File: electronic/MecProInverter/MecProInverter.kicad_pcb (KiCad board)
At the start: 4 copper layers, 104 x 175 mm, 167 parts, among them J10 Net, J3 ISO_Data, J4 Motor, J5 Display, J6 MAX312820, J7 Test, J8 U_ZK, J9 U_VS, K2 RT314A12, Q1 DMN3404L, Q2 DMN3404L, SW1 PTS645SM95SMTR92LFS, SW2 PTS645SM95SMTR92LFS, SW3 PTS645SM95SMTR92LFS, U1 ESP32-S3-MINI-1-N8, U10 CC6904SO-30A, U11 CC6904SO-30A, U12 TEA1-0505HI, U13 IKCM20L60GA, U14 PSRV05-4MR6T1G, U15 ADUM1201ARZ-RL7, U16 ADUM1201ARZ-RL7, U17 PSRV05-4MR6T1G, U18 PMV100EPAR, U19 PSRV05-4MR6T1G, U2 ADUM3160, U20 PSRV05-4MR6T1G, U3 TYPE-C_16PIN_2MD(073), U4 LVE2560E, U5 TPS563201DDCR, U6 SKRKAEE020, U7 SKRKAEE020, U8 TLA2528IRTER, U9 CC6904SO-30A

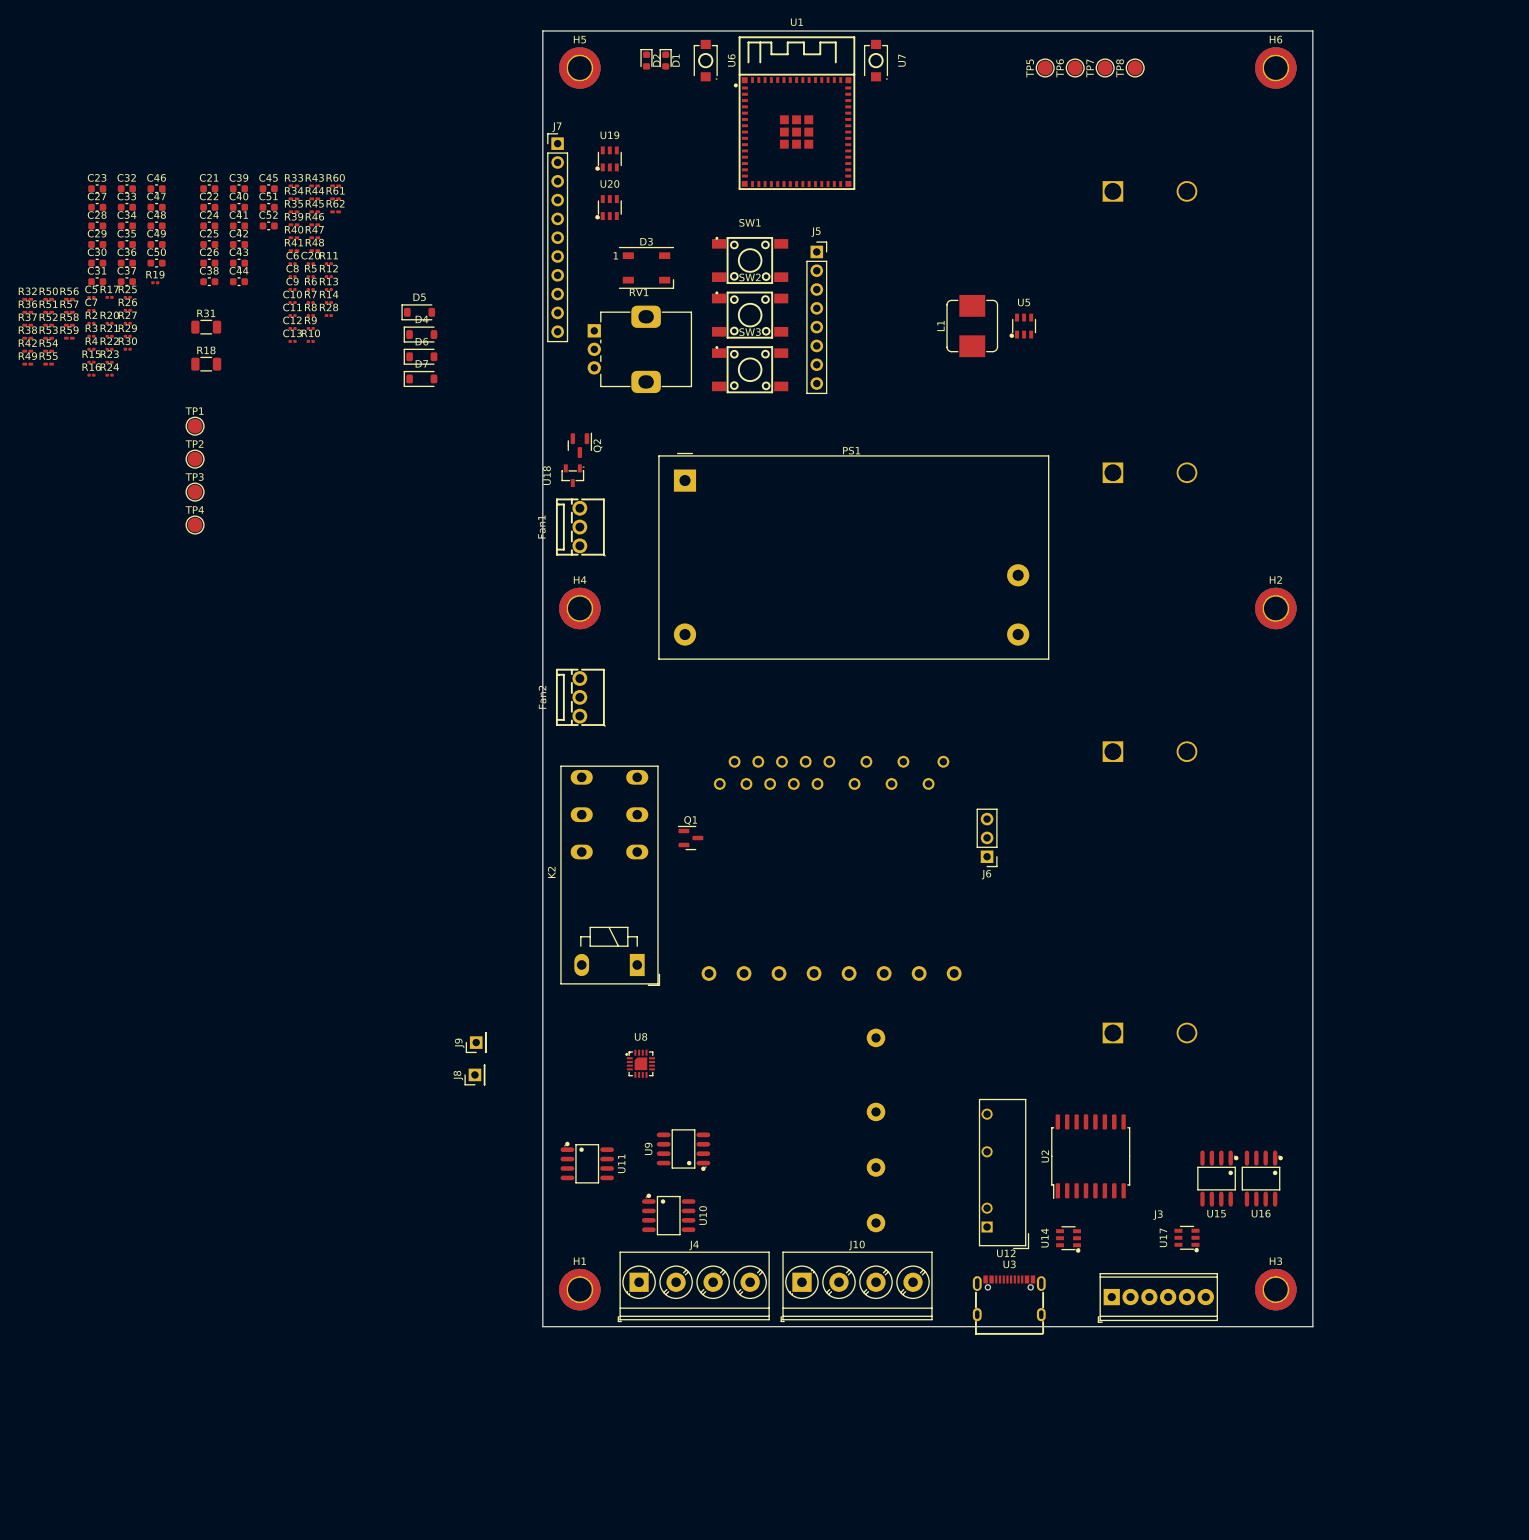
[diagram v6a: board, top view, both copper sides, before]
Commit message: Electronic
Voltage messurment updated
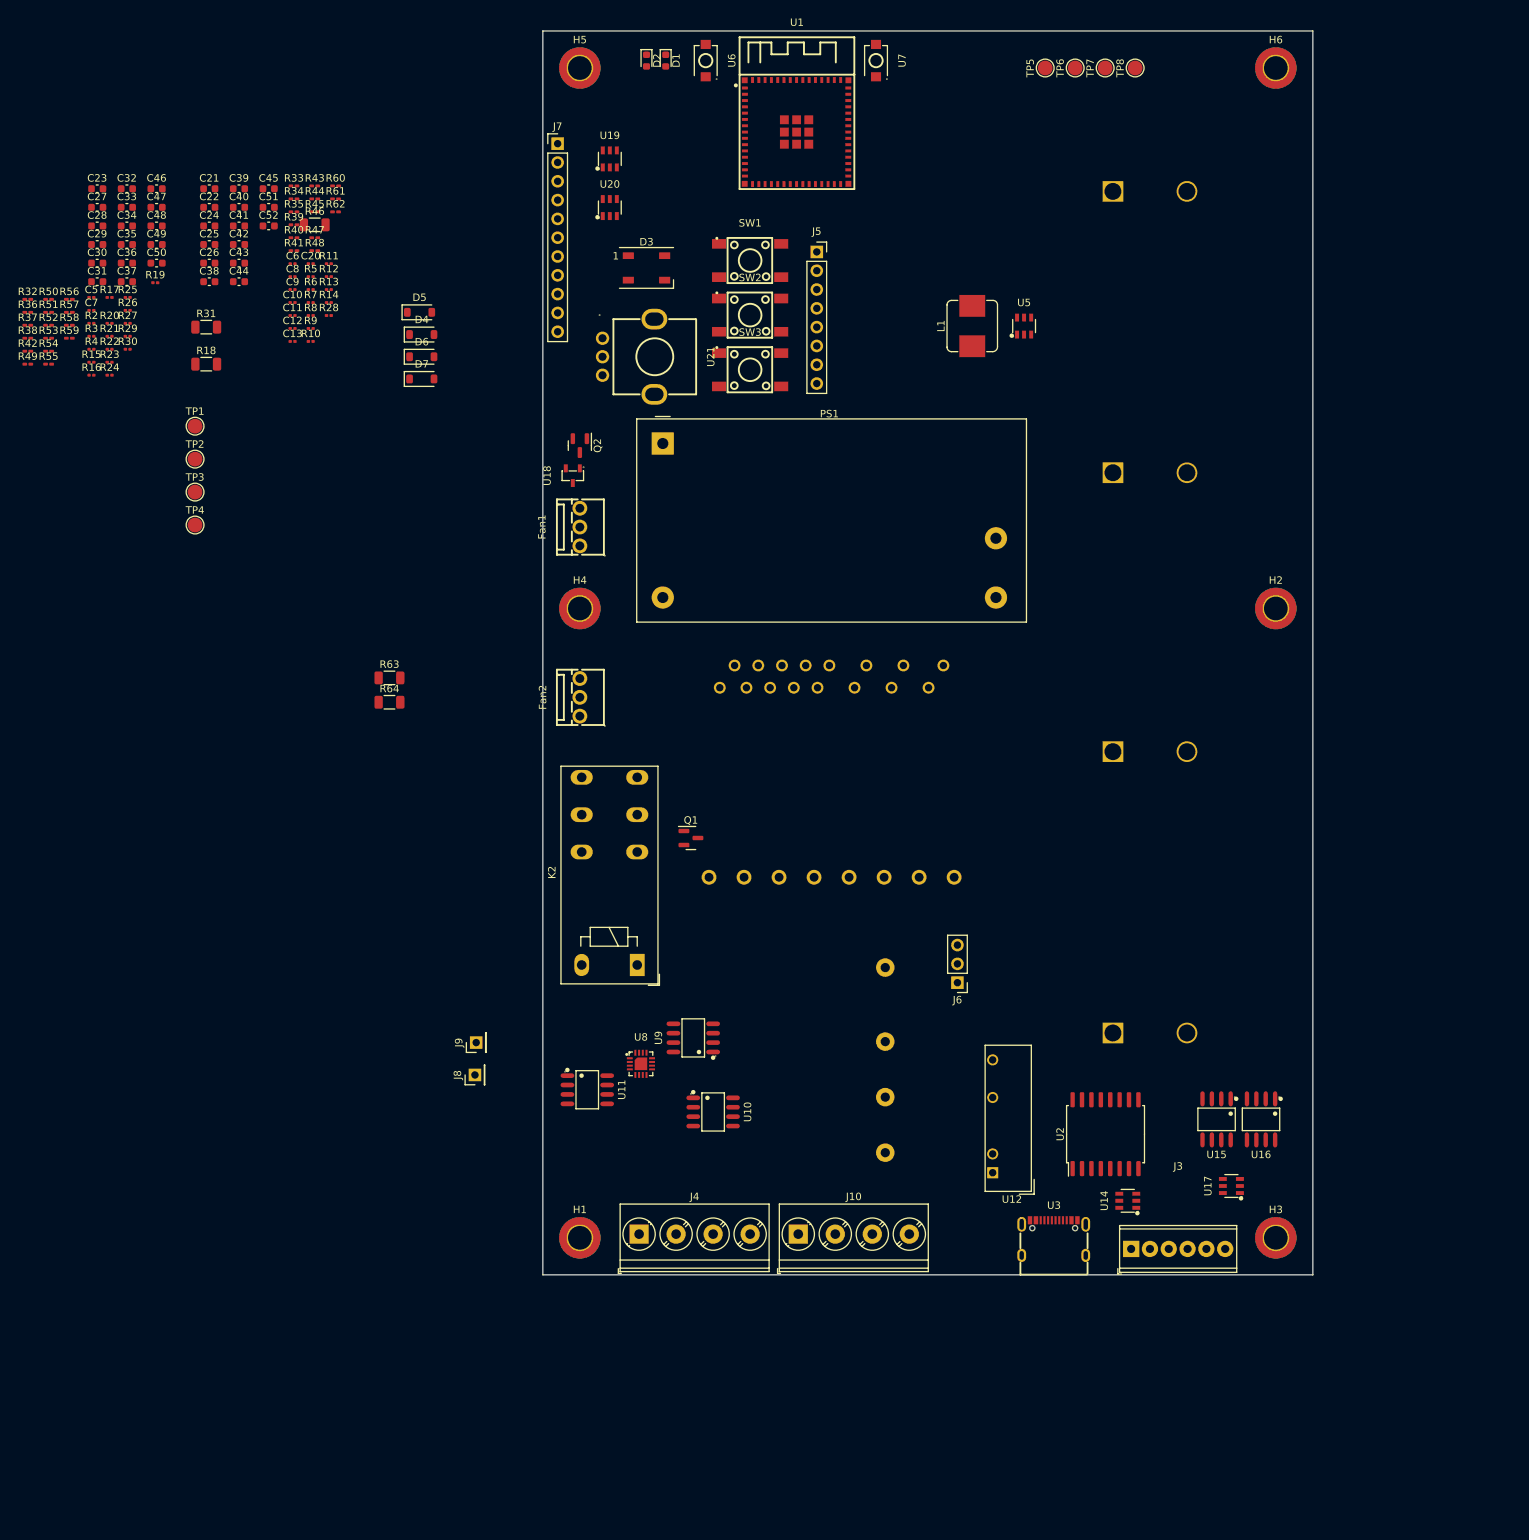
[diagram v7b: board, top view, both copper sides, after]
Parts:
- removed RV1: 10K, Potentiometer_THT:Potentiometer_Alps_RK09K_Single_Vertical
- added R63: 33k, Resistor_SMD:R_1206_3216Metric, F.Cu at (73.3, 140.4)
- added R64: 33k, Resistor_SMD:R_1206_3216Metric, F.Cu at (73.3, 143.7)
- added U21: RK09D113000F_10k, footprint:RES-ADJ-TH_RK09D1130C4G, F.Cu at (105.6, 97.0)
- R41: value 10k -> 4,7k
- R46: value 100k -> 33k; footprint Resistor_SMD:R_0201_0603Metric_Pad0.64x0.40mm_HandSolder -> Resistor_SMD:R_1206_3216Metric
- moved J6 17.5 mm to (150.0, 181.5)
- moved U10 15.2 mm to (117.0, 199.0)
- moved U9 15.1 mm to (114.3, 189.0)
- moved U13 13.0 mm to (133.0, 153.0)
- moved U11 10.0 mm to (100.0, 196.0)
- moved U3 10.0 mm to (163.0, 216.0)
- moved U4 9.58 mm to (140.2, 179.5)
- moved U14 9.46 mm to (173.0, 211.0)
- moved U17 9.22 mm to (187.0, 209.0)
- moved U15 8.00 mm to (185.0, 200.0)
- moved U16 8.00 mm to (191.0, 200.0)
- moved U12 7.37 mm to (154.8, 207.2)
- moved J3 7.01 mm to (173.5, 217.5)
- moved H1 7.00 mm to (99.0, 216.0)
- moved H3 7.00 mm to (193.0, 216.0)
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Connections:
- C51 pad 1: ITRIP -> Net-(U13-ITRIP)
- K2 pad 14: Net-(K2-Pad14) -> Net-(U4-~Phase)
- R41 pad 2: ITRIP -> Net-(U13-ITRIP)
- R46 pad 1: Net-(J8-Pin_1) -> Net-(R46-Pad1)
- R46 pad 2: Net-(U8-AIN2/GPIO2) -> Net-(R46-Pad2)
- U1 pad 27: VFO -> /Control/FAN2_PWM_FB
- U1 pad 30: unconnected-(U1-IO48-Pad30) -> /Control/FAN1_PWM_FB
- U1 pad 6: /Control/FAN1_PWM_FB -> VFO
- U1 pad 7: /Control/FAN2_PWM_FB -> unconnected-(U1-IO3-Pad7)
- U13 pad 15: ITRIP -> Net-(U13-ITRIP)
- U4 pad 1: Net-(J8-Pin_1) -> Net-(U4-VDD)
- U9 pad 1: Net-(K2-Pad14) -> Net-(U4-VDD)
- U9 pad 2: Net-(K2-Pad14) -> Net-(U4-VDD)
- U9 pad 3: Net-(U4-~Phase) -> Net-(J8-Pin_1)
- U9 pad 4: Net-(U4-~Phase) -> Net-(J8-Pin_1)
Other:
- board size 104 x 175 mm -> 104 x 168 mm

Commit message: Electronic
docu
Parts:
- C1, C2, C3, C4: footprint footprints:ESMQ351VSN102MA50S -> Own_Footprint:ESMQ351VSN102MA50S
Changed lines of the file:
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@@
     )
   )
-  (footprint "footprints:ESMQ351VSN102MA50S" locked (layer "B.Cu")
+  (footprint "Own_Footprint:ESMQ351VSN102MA50S" locked (layer "B.Cu")
     (at 171 112.66675 90)
     (tags "ESMQ351VSN102MA50S ")
     (property "Sheetfile" "power.kicad_sch")
     (property "Sheetname" "Power")
-    (property "ki_description" "Unpolarized capacitor")
+    (property "ki_description" "Polarized capacitor")
     (property "ki_keywords" "cap capacitor")
     (attr through_hole)
@@
     (pad "2" thru_hole circle locked (at 0 10 90) (size 2.794 2.794) (drill 2.286) (layers "*.Cu" "*.Mask")
       (net 2 "GND") (pintype "passive"))
-  )
-  (footprint "footprints:ESMQ351VSN102MA50S" locked (layer "B.Cu")
+    (model "C:/GitHub/MecProInverter/electronic/own_library/footprint/packages3d/ESMQ351VSN102MA50S.stp"
+      (offset (xyz 0 5 0))
+      (scale (xyz 1 1 1))
+      (rotate (xyz 0 0 0))
+    )
+  )
+  (footprint "Own_Footprint:ESMQ351VSN102MA50S" locked (layer "B.Cu")
     (at 171 74.66675 90)
     (tags "ESMQ351VSN102MA50S ")
     (property "Sheetfile" "power.kicad_sch")
     (property "Sheetname" "Power")
-    (property "ki_description" "Unpolarized capacitor")
-    (property "ki_keywords" "cap capacitor")
-    (attr through_hole)
-    (fp_text reference "C1" (at 1.66675 5 270 unlocked) (layer "B.SilkS")
-        (effects (font (size 1 1) (thickness 0.15)) (justify mirror))
-    )
-    (fp_text value "1mF" (at 1.66675 5 270 unlocked) (layer "B.Fab")
-        (effects (font (size 1 1) (thickness 0.15)) (justify mirror))
-    )
-    (fp_text user "${REFERENCE}" (at 1.66675 5 270 unlocked) (layer "B.Fab")
-        (effects (font (size 1 1) (thickness 0.15)) (justify mirror))
-    )
-    (fp_line (start 17.7546 0) (end 19.0246 0)
-      (stroke (width 0.1524) (type solid)) (layer "B.SilkS"))
-    (fp_line (start 18.3896 0.635) (end 18.3896 -0.635)
-      (stroke (width 0.1524) (type solid)) (layer "B.SilkS"))
-    (fp_circle (center 0 5) (end 17.6276 5)
-      (stroke (width 0.1524) (type solid)) (fill none) (layer "B.SilkS"))
-    (fp_circle (center 0 5) (end 5 5)
-      (stroke (width 0.0254) (type solid)) (fill none) (layer "Dwgs.User"))
-    (fp_line (start -17.7546 -2.310716) (end -17.7546 12.310717)
-      (stroke (width 0.0254) (type solid)) (layer "B.CrtYd"))
-    (fp_line (start -17.7546 12.310717) (end -7.310717 22.7546)
-      (stroke (width 0.0254) (type solid)) (layer "B.CrtYd"))
-    (fp_line (start -7.310717 -12.7546) (end -17.7546 -2.310716)
-      (stroke (width 0.0254) (type solid)) (layer "B.CrtYd"))
-    (fp_line (start -7.310717 22.7546) (end 7.310717 22.7546)
-      (stroke (width 0.0254) (type solid)) (layer "B.CrtYd"))
-    (fp_line (start 7.310717 -12.7546) (end -7.310717 -12.7546)
-      (stroke (width 0.0254) (type solid)) (layer "B.CrtYd"))
-    (fp_line (start 7.310717 22.7546) (end 17.7546 12.310717)
-      (stroke (width 0.0254) (type solid)) (layer "B.CrtYd"))
-    (fp_line (start 17.7546 -2.310716) (end 7.310717 -12.7546)
-      (stroke (width 0.0254) (type solid)) (layer "B.CrtYd"))
-    (fp_line (start 17.7546 12.310717) (end 17.7546 -2.310716)
-      (stroke (width 0.0254) (type solid)) (layer "B.CrtYd"))
-    (fp_line (start 17.7546 0) (end 19.0246 0)
-      (stroke (width 0.0254) (type solid)) (layer "B.Fab"))
-    (fp_line (start 18.3896 0.635) (end 18.3896 -0.635)
-      (stroke (width 0.0254) (type solid)) (layer "B.Fab"))
-    (fp_circle (center 0 5) (end 17.5006 5)
-      (stroke (width 0.0254) (type solid)) (fill none) (layer "B.Fab"))
-    (pad "1" thru_hole rect locked (at 0 0 90) (size 2.794 2.794) (drill 2.286) (layers "*.Cu" "*.Mask")
-      (net 26 "Net-(J8-Pin_1)") (pintype "passive"))
-    (pad "2" thru_hole circle locked (at 0 10 90) (size 2.794 2.794) (drill 2.286) (layers "*.Cu" "*.Mask")
-      (net 2 "GND") (pintype "passive"))
-  )
-  (footprint "footprints:ESMQ351VSN102MA50S" locked (layer "B.Cu")
+    (property "ki_description" "Polarized capacitor")
+    (property "ki_keywords" "cap capacitor")
+    (attr through_hole)
+    (fp_text reference "C1" (at 0 5 270 unlocked) (layer "B.SilkS")
+        (effects (font (size 1 1) (thickness 0.15)) (justify mirror))
+    )
+    (fp_text value "1mF" (at 0 5 270 unlocked) (layer "B.Fab")
+        (effects (font (size 1 1) (thickness 0.15)) (justify mirror))
+    )
+    (fp_text user "${REFERENCE}" (at 0 5 270 unlocked) (layer "B.Fab")
+        (effects (font (size 1 1) (thickness 0.15)) (justify mirror))
+    )
+    (fp_line (start 17.7546 0) (end 19.0246 0)
+      (stroke (width 0.1524) (type solid)) (layer "B.SilkS"))
+    (fp_line (start 18.3896 0.635) (end 18.3896 -0.635)
+      (stroke (width 0.1524) (type solid)) (layer "B.SilkS"))
+    (fp_circle (center 0 5) (end 17.6276 5)
+      (stroke (width 0.1524) (type solid)) (fill none) (layer "B.SilkS"))
+    (fp_circle (center 0 5) (end 5 5)
+      (stroke (width 0.0254) (type solid)) (fill none) (layer "Dwgs.User"))
+    (fp_line (start -17.7546 -2.310716) (end -17.7546 12.310717)
+      (stroke (width 0.0254) (type solid)) (layer "B.CrtYd"))
+    (fp_line (start -17.7546 12.310717) (end -7.310717 22.7546)
+      (stroke (width 0.0254) (type solid)) (layer "B.CrtYd"))
+    (fp_line (start -7.310717 -12.7546) (end -17.7546 -2.310716)
+      (stroke (width 0.0254) (type solid)) (layer "B.CrtYd"))
+    (fp_line (start -7.310717 22.7546) (end 7.310717 22.7546)
+      (stroke (width 0.0254) (type solid)) (layer "B.CrtYd"))
+    (fp_line (start 7.310717 -12.7546) (end -7.310717 -12.7546)
+      (stroke (width 0.0254) (type solid)) (layer "B.CrtYd"))
+    (fp_line (start 7.310717 22.7546) (end 17.7546 12.310717)
+      (stroke (width 0.0254) (type solid)) (layer "B.CrtYd"))
+    (fp_line (start 17.7546 -2.310716) (end 7.310717 -12.7546)
+      (stroke (width 0.0254) (type solid)) (layer "B.CrtYd"))
+    (fp_line (start 17.7546 12.310717) (end 17.7546 -2.310716)
+      (stroke (width 0.0254) (type solid)) (layer "B.CrtYd"))
+    (fp_line (start 17.7546 0) (end 19.0246 0)
+      (stroke (width 0.0254) (type solid)) (layer "B.Fab"))
+    (fp_line (start 18.3896 0.635) (end 18.3896 -0.635)
+      (stroke (width 0.0254) (type solid)) (layer "B.Fab"))
+    (fp_circle (center 0 5) (end 17.5006 5)
+      (stroke (width 0.0254) (type solid)) (fill none) (layer "B.Fab"))
+    (pad "1" thru_hole rect locked (at 0 0 90) (size 2.794 2.794) (drill 2.286) (layers "*.Cu" "*.Mask")
+      (net 26 "Net-(J8-Pin_1)") (pintype "passive"))
+    (pad "2" thru_hole circle locked (at 0 10 90) (size 2.794 2.794) (drill 2.286) (layers "*.Cu" "*.Mask")
+      (net 2 "GND") (pintype "passive"))
+    (model "C:/GitHub/MecProInverter/electronic/own_library/footprint/packages3d/ESMQ351VSN102MA50S.stp"
+      (offset (xyz 0 5 0))
+      (scale (xyz 1 1 1))
+      (rotate (xyz 0 0 0))
+    )
+  )
+  (footprint "Own_Footprint:ESMQ351VSN102MA50S" locked (layer "B.Cu")
     (at 171 188.3335 90)
     (tags "ESMQ351VSN102MA50S ")
     (property "Sheetfile" "power.kicad_sch")
     (property "Sheetname" "Power")
-    (property "ki_description" "Unpolarized capacitor")
+    (property "ki_description" "Polarized capacitor")
     (property "ki_keywords" "cap capacitor")
     (attr through_hole)
@@
     (pad "2" thru_hole circle locked (at 0 10 90) (size 2.794 2.794) (drill 2.286) (layers "*.Cu" "*.Mask")
       (net 2 "GND") (pintype "passive"))
-  )
-  (footprint "footprints:ESMQ351VSN102MA50S" locked (layer "B.Cu")
+    (model "C:/GitHub/MecProInverter/electronic/own_library/footprint/packages3d/ESMQ351VSN102MA50S.stp"
+      (offset (xyz 0 5 0))
+      (scale (xyz 1 1 1))
+      (rotate (xyz 0 0 0))
+    )
+  )
+  (footprint "Own_Footprint:ESMQ351VSN102MA50S" locked (layer "B.Cu")
     (at 171 150.3335 90)
     (tags "ESMQ351VSN102MA50S ")
     (property "Sheetfile" "power.kicad_sch")
     (property "Sheetname" "Power")
-    (property "ki_description" "Unpolarized capacitor")
+    (property "ki_description" "Polarized capacitor")
     (property "ki_keywords" "cap capacitor")
     (attr through_hole)
@@
     (pad "2" thru_hole circle locked (at 0 10 90) (size 2.794 2.794) (drill 2.286) (layers "*.Cu" "*.Mask")
       (net 2 "GND") (pintype "passive"))
+    (model "C:/GitHub/MecProInverter/electronic/own_library/footprint/packages3d/ESMQ351VSN102MA50S.stp"
+      (offset (xyz 0 5 0))
+      (scale (xyz 1 1 1))
+      (rotate (xyz 0 0 0))
+    )
   )
   (footprint "footprint:DIP-24_L36.0-W21.0-P1.60-LS28.6-TL" (layer "B.Cu")
